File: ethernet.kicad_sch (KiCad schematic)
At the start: 45 parts, among them J5 ARJM11D7-502-AB-EW2, U1 MIMX8MM6DVTLZAA, U21 RTL8211FD, U22 TPD4E02B04, U23 TPD4E02B04, Y2 25MHz

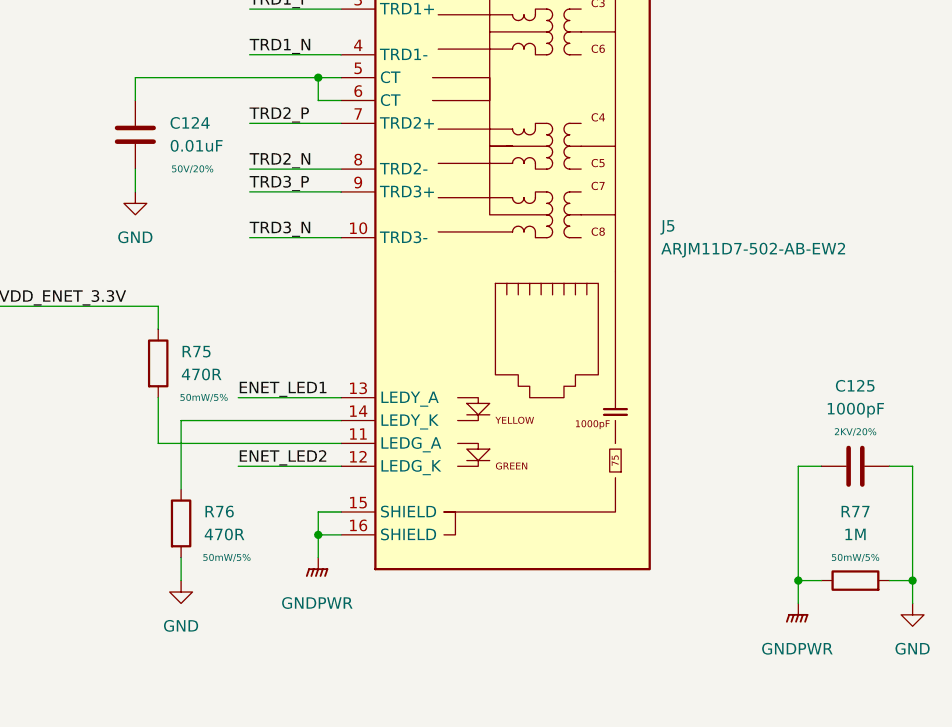
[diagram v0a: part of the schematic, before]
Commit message: bom work, change uart level shifter and m.2 socket
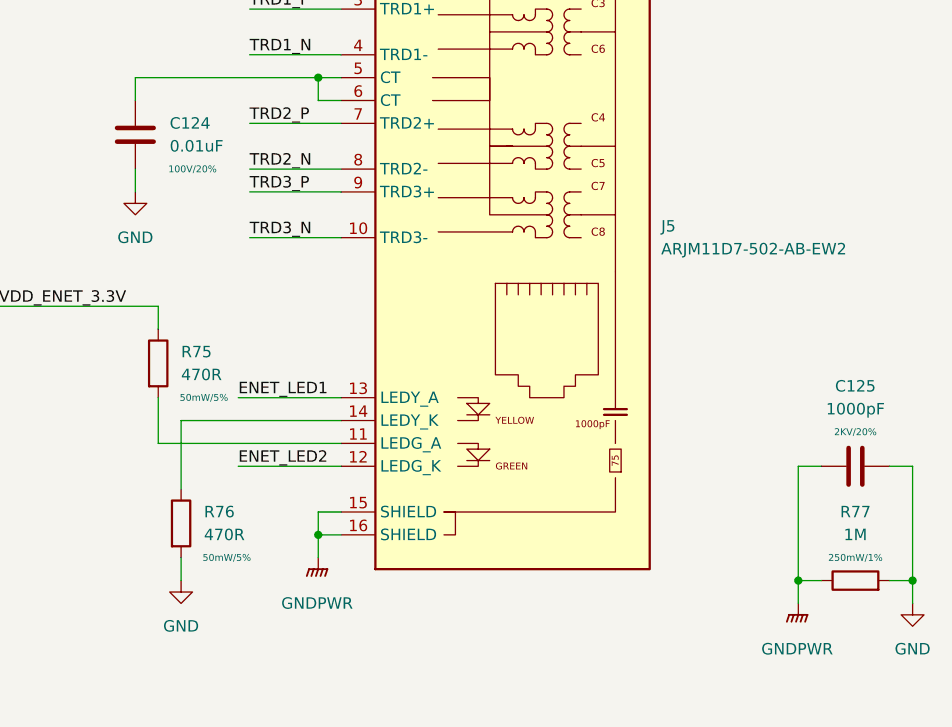
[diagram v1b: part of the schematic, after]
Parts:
- C112, C113, C114, C115, C117, C118, C119, C121, C123: MPN (none) -> CL05A104KA5NNNC
- C116: MPN (none) -> CL05A475MP5NRNC
- C120, C122: MPN (none) -> 04025U140FAT2A
- C124: MPN (none) -> GCM188R72A103KA37D; Rating 50V/20% -> 100V/20%
- C125: MPN (none) -> C1210C102KGRAC7800
- J5: MPN (none) -> ARJM11D7-502-AB-EW2
- R53, R54, R55, R56, R57, R58, R59, R60, R61: MPN (none) -> RC0201FR-074K7L
- R62, R63, R71, R72, R73, R74: MPN (none) -> RC0402JR-074K7L
- R64: MPN (none) -> RC0402FR-071K5L
- R65, R66, R67, R68, R69: MPN (none) -> RC0402FR-070RL
- R70: MPN (none) -> RC0402FR-072K49L
- R75, R76: MPN (none) -> RC0402FR-07470RL
- R77: MPN (none) -> RC1206FR-071ML; Rating 50mW/5% -> 250mW/1%
- U1: MPN (none) -> MIMX8MM6DVTLZAA
- U21: MPN (none) -> RTL8211FD-CG
- U22, U23: MPN (none) -> TPD4E02B04DQAR

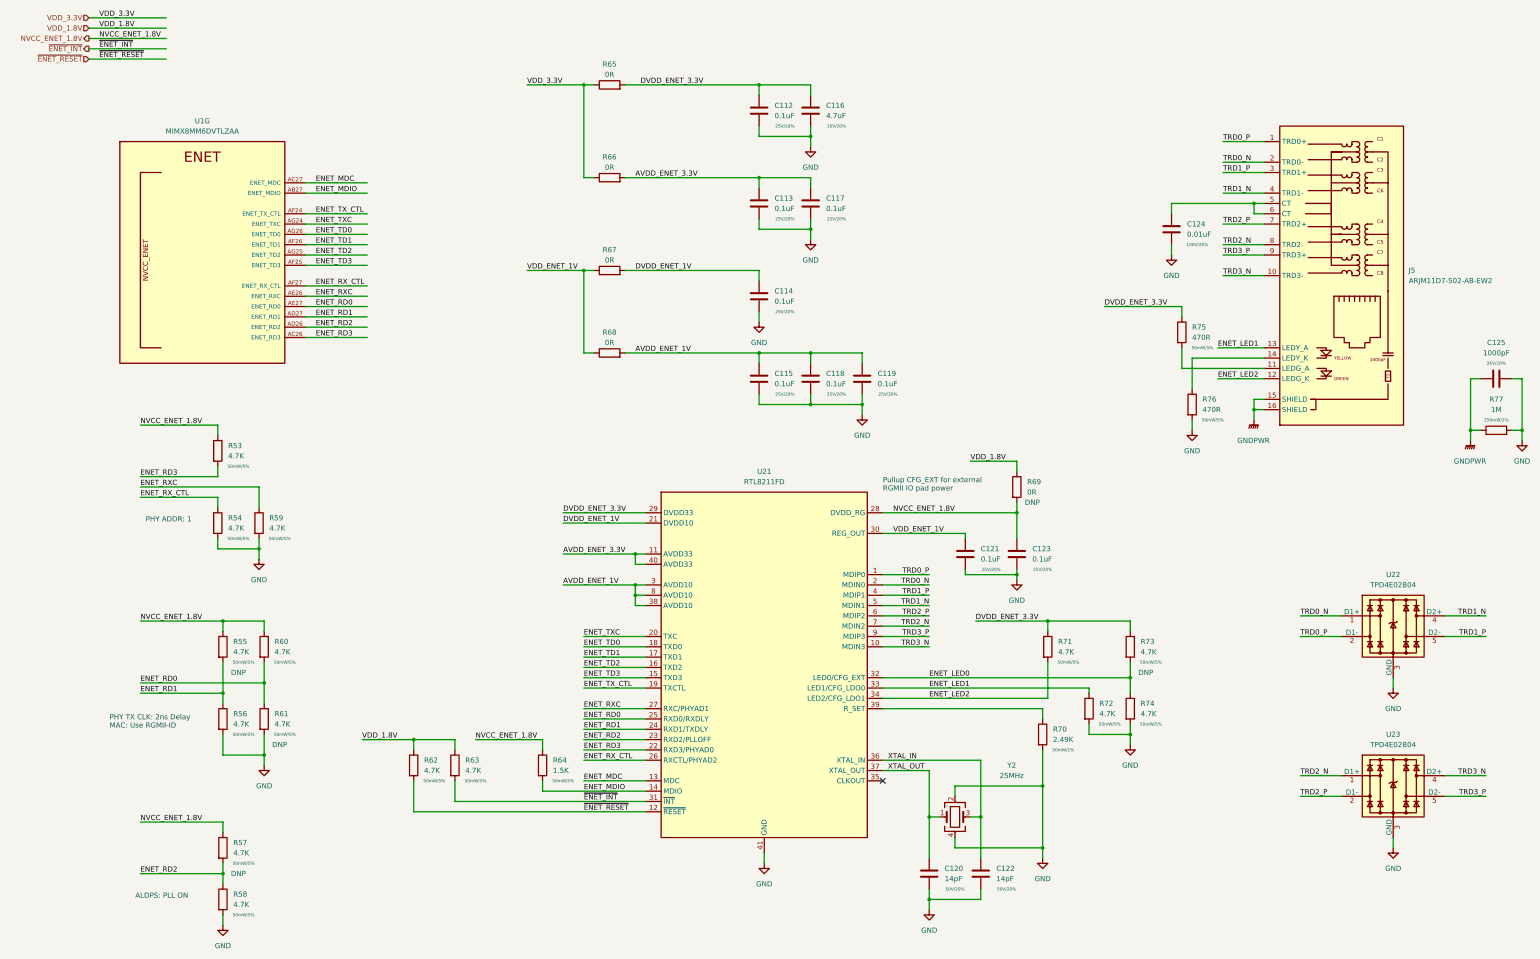
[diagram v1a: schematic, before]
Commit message: ddr length matching work, misc cleanup
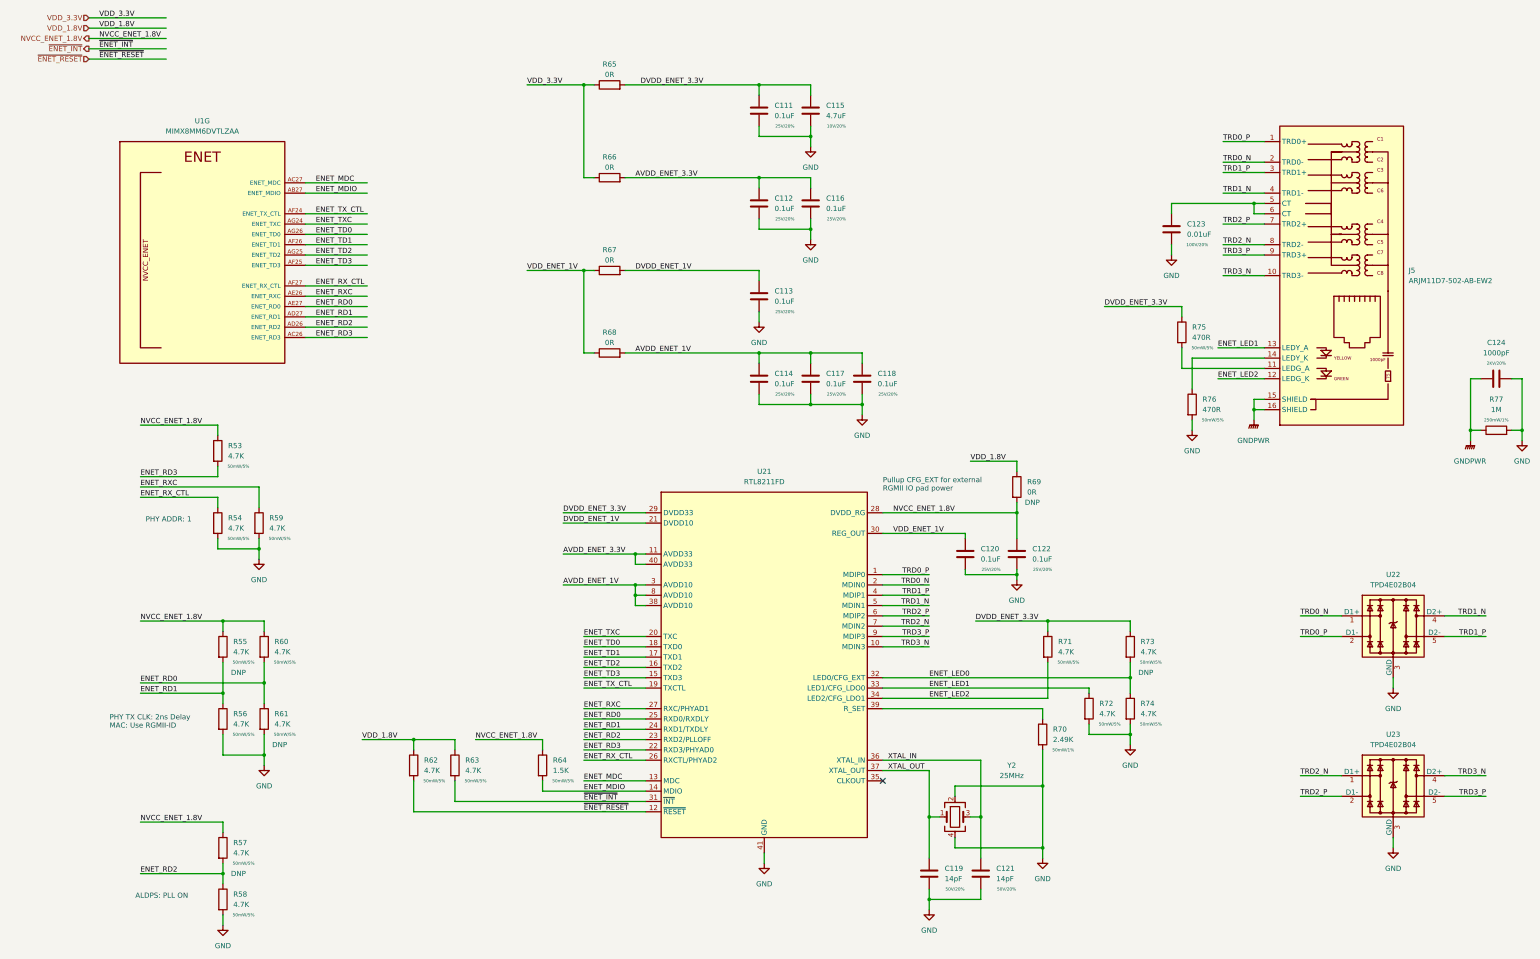
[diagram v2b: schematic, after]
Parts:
- renumbered C112 to C111, C113 to C112, C114 to C113, C115 to C114, C116 to C115, C117 to C116, C118 to C117, C119 to C118, C120 to C119, C121 to C120, C122 to C121, C123 to C122, C124 to C123, C125 to C124
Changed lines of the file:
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@@
   (symbol (lib_id "Device:C") (at 198.12 109.22 0) (unit 1)
     (in_bom yes) (on_board yes)
-    (property "Reference" "C115" (id 0) (at 201.93 107.9499 0)
+    (property "Reference" "C114" (id 0) (at 201.93 107.9499 0)
       (effects (font (size 1.27 1.27)) (justify left))
     )
@@
   (symbol (lib_id "Device:C") (at 210.82 43.18 0) (unit 1)
     (in_bom yes) (on_board yes)
-    (property "Reference" "C116" (id 0) (at 214.63 41.9099 0)
+    (property "Reference" "C115" (id 0) (at 214.63 41.9099 0)
       (effects (font (size 1.27 1.27)) (justify left))
     )
@@
   (symbol (lib_id "Device:C") (at 379.73 109.22 90) (unit 1)
     (in_bom yes) (on_board yes)
-    (property "Reference" "C125" (id 0) (at 379.73 100.33 90))
+    (property "Reference" "C124" (id 0) (at 379.73 100.33 90))
     (property "Value" "1000pF" (id 1) (at 379.73 102.87 90))
     (property "Footprint" "Capacitor_SMD:C_1210_3225Metric" (id 2) (at 383.54 108.2548 0)
@@
   (symbol (lib_id "Device:C") (at 248.92 152.4 0) (unit 1)
     (in_bom yes) (on_board yes)
-    (property "Reference" "C121" (id 0) (at 252.73 151.1299 0)
+    (property "Reference" "C120" (id 0) (at 252.73 151.1299 0)
       (effects (font (size 1.27 1.27)) (justify left))
     )
@@
   (symbol (lib_id "Device:C") (at 240.03 231.14 0) (unit 1)
     (in_bom yes) (on_board yes)
-    (property "Reference" "C120" (id 0) (at 243.84 229.8699 0)
+    (property "Reference" "C119" (id 0) (at 243.84 229.8699 0)
       (effects (font (size 1.27 1.27)) (justify left))
     )
@@
   (symbol (lib_id "Device:C") (at 198.12 66.04 0) (unit 1)
     (in_bom yes) (on_board yes)
-    (property "Reference" "C113" (id 0) (at 201.93 64.7699 0)
+    (property "Reference" "C112" (id 0) (at 201.93 64.7699 0)
       (effects (font (size 1.27 1.27)) (justify left))
     )
@@
   (symbol (lib_id "Device:C") (at 261.62 152.4 0) (unit 1)
     (in_bom yes) (on_board yes)
-    (property "Reference" "C123" (id 0) (at 265.43 151.1299 0)
+    (property "Reference" "C122" (id 0) (at 265.43 151.1299 0)
       (effects (font (size 1.27 1.27)) (justify left))
     )
@@
   (symbol (lib_id "Device:C") (at 299.72 72.39 0) (unit 1)
     (in_bom yes) (on_board yes)
-    (property "Reference" "C124" (id 0) (at 303.53 71.1199 0)
+    (property "Reference" "C123" (id 0) (at 303.53 71.1199 0)
       (effects (font (size 1.27 1.27)) (justify left))
     )
@@
   (symbol (lib_id "Device:C") (at 198.12 88.9 0) (unit 1)
     (in_bom yes) (on_board yes)
-    (property "Reference" "C114" (id 0) (at 201.93 87.6299 0)
+    (property "Reference" "C113" (id 0) (at 201.93 87.6299 0)
       (effects (font (size 1.27 1.27)) (justify left))
     )
@@
   (symbol (lib_id "Device:C") (at 223.52 109.22 0) (unit 1)
     (in_bom yes) (on_board yes)
-    (property "Reference" "C119" (id 0) (at 227.33 107.9499 0)
+    (property "Reference" "C118" (id 0) (at 227.33 107.9499 0)
       (effects (font (size 1.27 1.27)) (justify left))
     )
@@
   (symbol (lib_id "Device:C") (at 210.82 109.22 0) (unit 1)
     (in_bom yes) (on_board yes)
-    (property "Reference" "C118" (id 0) (at 214.63 107.9499 0)
+    (property "Reference" "C117" (id 0) (at 214.63 107.9499 0)
       (effects (font (size 1.27 1.27)) (justify left))
     )
@@
   (symbol (lib_id "Device:C") (at 210.82 66.04 0) (unit 1)
     (in_bom yes) (on_board yes)
-    (property "Reference" "C117" (id 0) (at 214.63 64.7699 0)
+    (property "Reference" "C116" (id 0) (at 214.63 64.7699 0)
       (effects (font (size 1.27 1.27)) (justify left))
     )
@@
   (symbol (lib_id "Device:C") (at 198.12 43.18 0) (unit 1)
     (in_bom yes) (on_board yes)
-    (property "Reference" "C112" (id 0) (at 201.93 41.9099 0)
+    (property "Reference" "C111" (id 0) (at 201.93 41.9099 0)
       (effects (font (size 1.27 1.27)) (justify left))
     )
@@
   (symbol (lib_id "Device:C") (at 252.73 231.14 0) (unit 1)
     (in_bom yes) (on_board yes)
-    (property "Reference" "C122" (id 0) (at 256.54 229.8699 0)
-      (effects (font (size 1.27 1.27)) (justify left))
-    )
+    (property "Reference" "C121" (id 0) (at 256.54 229.8699 0)
+      (effects (font (size 1.27 1.27)) (justify left))
+    )

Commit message: misc cleanup, change from usb mux to dual uart
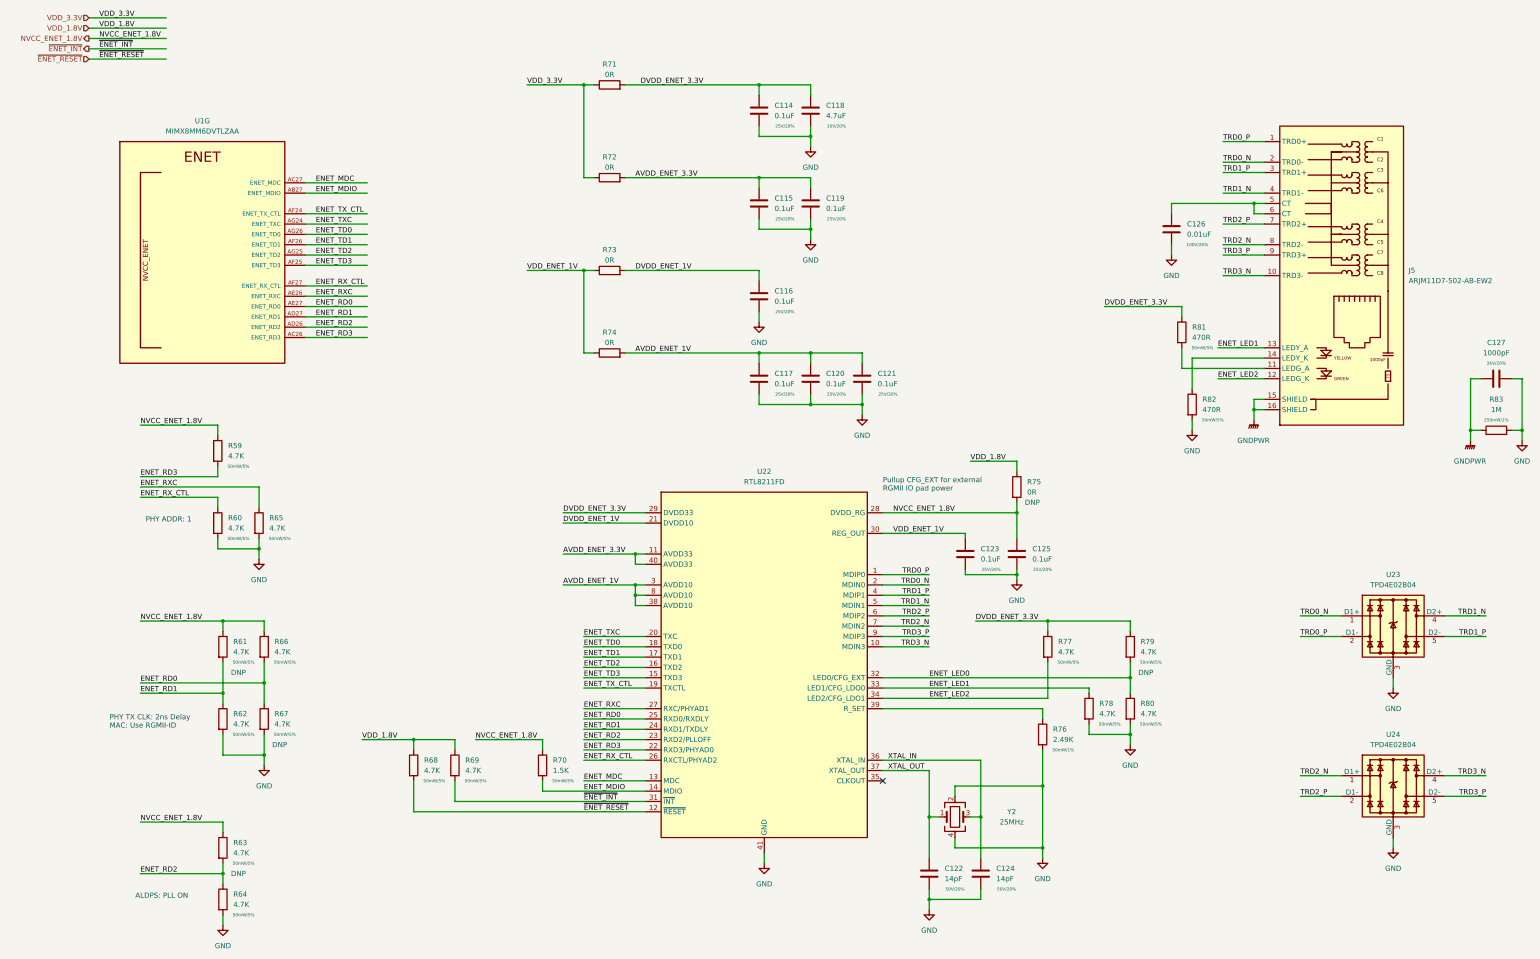
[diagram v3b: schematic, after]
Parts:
- renumbered C111 to C114, C112 to C115, C113 to C116, C114 to C117, C115 to C118, C116 to C119, C117 to C120, C118 to C121, C119 to C122, C120 to C123, C121 to C124, C122 to C125, C123 to C126, C124 to C127, R53 to R59, R54 to R60, R55 to R61, R56 to R62, R57 to R63, R58 to R64, R59 to R65, R60 to R66, R61 to R67, R62 to R68, R63 to R69, R64 to R70, R65 to R71, R66 to R72, R67 to R73, R68 to R74, R69 to R75, R70 to R76, R71 to R77, R72 to R78, R73 to R79, R74 to R80, R75 to R81, R76 to R82, R77 to R83, U21 to U22, U22 to U23, U23 to U24

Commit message: Rev 1
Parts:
- removed C127: 1000pF, Capacitor_SMD:C_1210_3225Metric, symbol Device:C
- removed R83: 1M, Resistor_SMD:R_1206_3216Metric, symbol Device:R
- renumbered C114 to C115, C115 to C116, C116 to C117, C117 to C118, C118 to C119, C119 to C120, C120 to C121, C121 to C122, C122 to C123, C123 to C124, C124 to C125, C125 to C126, C126 to C127
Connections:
- net GNDPWR is gone; now on net GND: J5.15 (SHIELD), J5.16 (SHIELD)
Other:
- note added: "CFG_LDO[1:0] 10 - 1.8V RGMII IO"

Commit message: misc changes for rev1
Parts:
- R61: DNP DNP -> (none); now left out of the parts list
- R62: DNP (none) -> DNP
- R63, R67, R79: now left out of the parts list
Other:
- note added: "RX/TX CLK: 2ns Delay"
- note removed: "PHY TX CLK: 2ns Delay MAC: Use RGMII-ID"
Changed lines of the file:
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@@
     (effects (font (size 1.27 1.27)) (justify left bottom))
   )
-  (text "PHY TX CLK: 2ns Delay\nMAC: Use RGMII-ID" (at 38.1 195.58 0)
+  (text "RX/TX CLK: 2ns Delay" (at 38.1 191.77 0)
     (effects (font (size 1.27 1.27)) (justify left bottom))
   )
@@
   )
   (symbol (lib_id "Device:R") (at 66.04 224.79 0) (unit 1)
-    (in_bom yes) (on_board yes)
+    (in_bom no) (on_board yes)
     (property "Reference" "R63" (id 0) (at 68.58 223.5199 0)
       (effects (font (size 1.27 1.27)) (justify left))
@@
   )
   (symbol (lib_id "Device:R") (at 289.56 175.26 0) (unit 1)
-    (in_bom yes) (on_board yes)
+    (in_bom no) (on_board yes)
     (property "Reference" "R79" (id 0) (at 292.1 173.9899 0)
       (effects (font (size 1.27 1.27)) (justify left))
@@
   )
   (symbol (lib_id "Device:R") (at 76.2 193.04 0) (unit 1)
-    (in_bom yes) (on_board yes)
+    (in_bom no) (on_board yes)
     (property "Reference" "R67" (id 0) (at 78.74 191.7699 0)
       (effects (font (size 1.27 1.27)) (justify left))
@@
       (effects (font (size 1.27 1.27)) hide)
     )
+    (property "DNP" "DNP" (id 6) (at 69.85 199.39 0))
     (pin "1")
     (pin "2")
@@
   )
   (symbol (lib_id "Device:R") (at 66.04 175.26 0) (unit 1)
-    (in_bom yes) (on_board yes)
+    (in_bom no) (on_board yes)
     (property "Reference" "R61" (id 0) (at 68.58 173.9899 0)
       (effects (font (size 1.27 1.27)) (justify left))
@@
       (effects (font (size 0.762 0.762)))
     )
-    (property "DNP" "DNP" (id 5) (at 69.85 181.61 0))
     (property "MPN" "RC0201FR-074K7L" (id 6) (at 66.04 175.26 0)
       (effects (font (size 1.27 1.27)) hide)
